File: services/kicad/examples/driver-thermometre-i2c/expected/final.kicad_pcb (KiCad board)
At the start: 2 copper layers, 40 x 40 mm, 10 parts, among them J1 CONN_5V_GND_SDA_SCL, U1 AMS1117-3.3

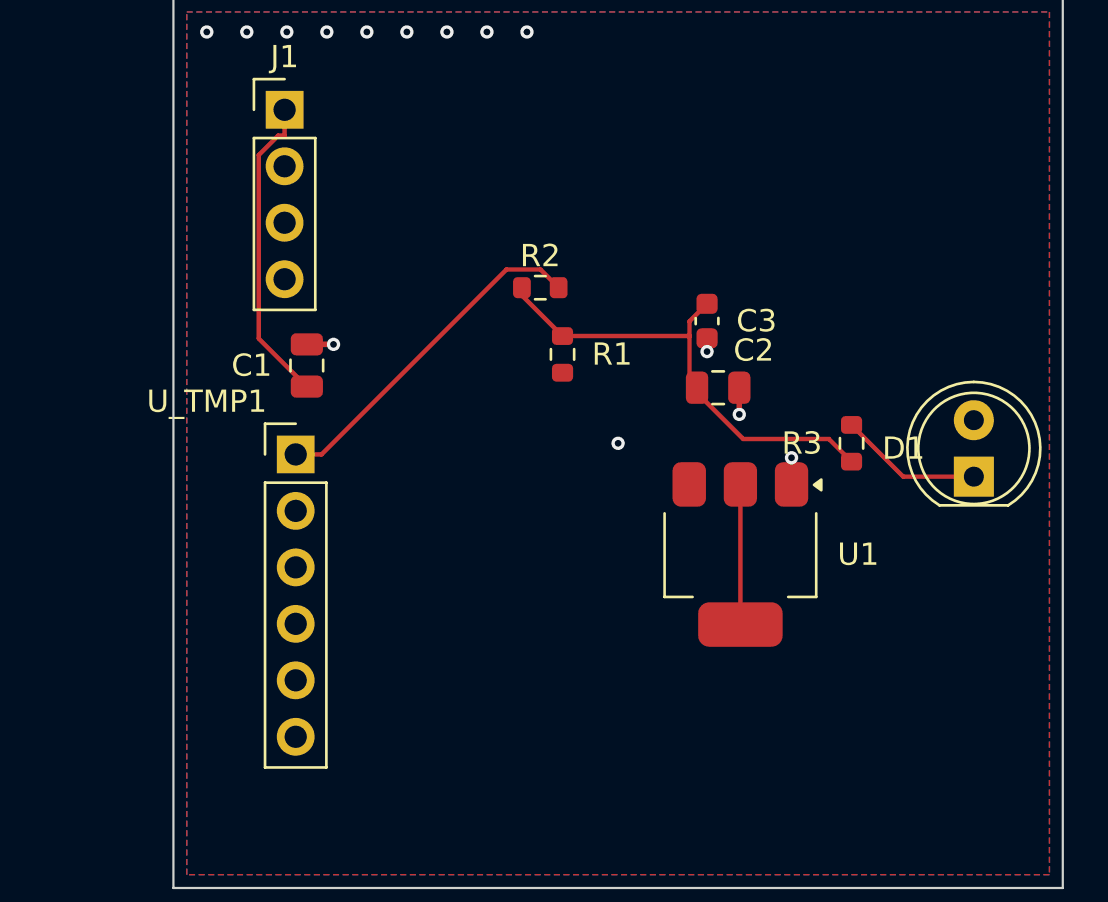
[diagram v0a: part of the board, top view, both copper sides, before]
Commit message: fix(agents): l'enrichissement ne reecrit plus un footprint deja qualifie ; exemple driver-thermometre-i2c sur le contrat durci
`quickLookup('J1', …)` rend un PinHeader 1x02 pour tout connecteur, quel que
soit l'indice : un footprint complet et juste (PinHeader_1x04) etait reecrit
en 1x02 dans l'etat publie et la BOM — le board, lui, gardait le bon. Un
footprint `Lib:Nom` ne se cherche plus.

Meme phrase rejouee sur le contrat durci (run 537dc8a5) : SDA passe de 1 a
3 broches, SCL de 2 a 3, 100 % route, 0 erreur, 198 s. README avant/apres.

Co-Authored-By: Claude Fable 5.1 <noreply@anthropic.com>
Claude-Session: https://claude.ai/code/session_01TnMqm4La2CxQHHB5K8aSSV
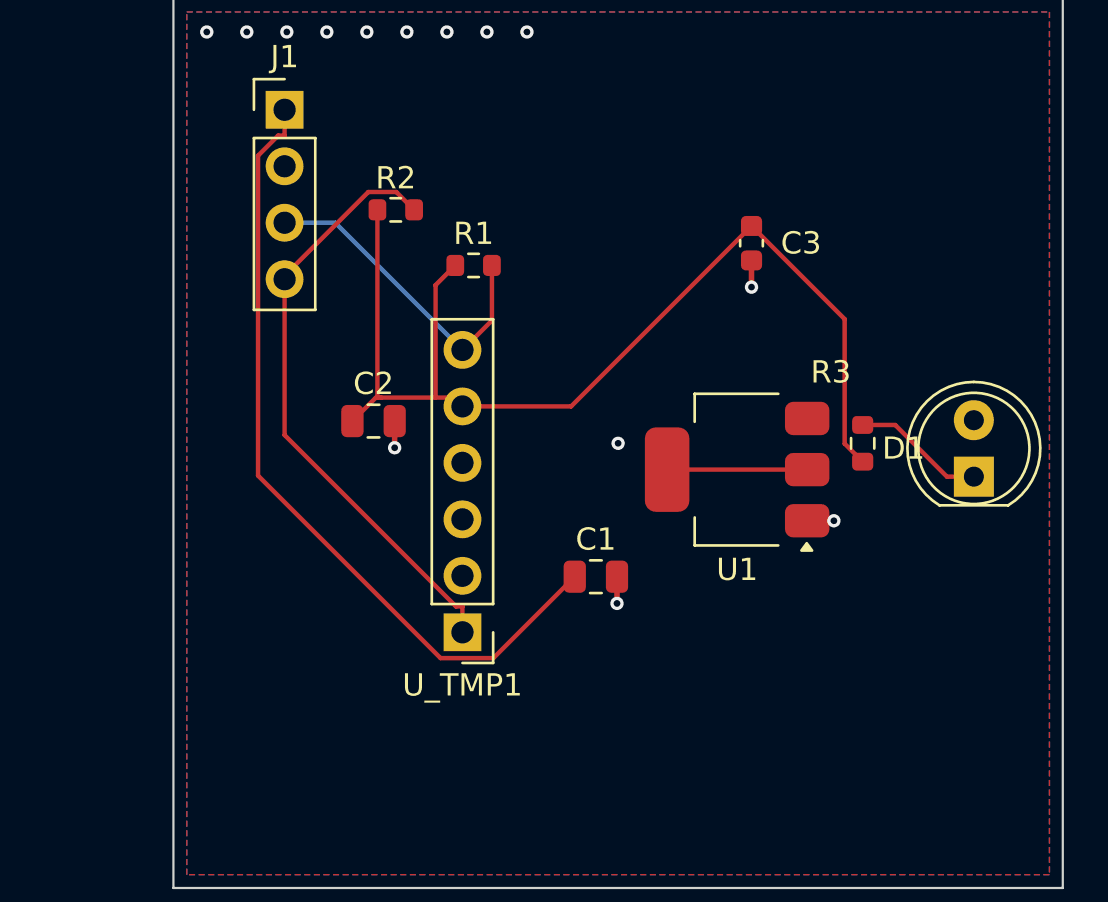
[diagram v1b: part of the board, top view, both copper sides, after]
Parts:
- J1: value CONN_5V_GND_SDA_SCL -> 5V_GND_SDA_SCL
- moved C1 16.1 mm to (147.5, 113.5), turned to 0 degrees
- moved C2 15.6 mm to (137.5, 106.5)
- moved U_TMP1 11.0 mm to (141.5, 116.0), turned to 180 degrees
- moved R2 7.38 mm to (138.5, 97.0)
- moved R1 5.66 mm to (142.0, 99.5), turned to 0 degrees
- moved C3 4.03 mm to (154.5, 98.5)
- moved U1 3.82 mm to (153.9, 108.7), turned to 180 degrees
- moved R3 0.50 mm to (159.5, 107.5)
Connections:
- J1 pad 3: Net-(J1-3) -> SDA
- J1 pad 4: Net-(J1-4) -> SCL
- U_TMP1 pad 4: Net-(U_TMP1-4) -> GND
- U_TMP1 pad 5: Net-(U_TMP1-5) -> +3V3
- U_TMP1 pad 6: Net-(U_TMP1-6) -> SDA
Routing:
- net +3V3: track 21.3 -> 49.3 mm
- net +5V: track 14.0 -> 36.3 mm
- net SDA: track 0.00 -> 14.7 mm
- net SCL: track 15.6 -> 27.2 mm
- net GND: track 4.20 -> 4.80 mm
- net NET_R3_D1: track 6.46 -> 5.96 mm

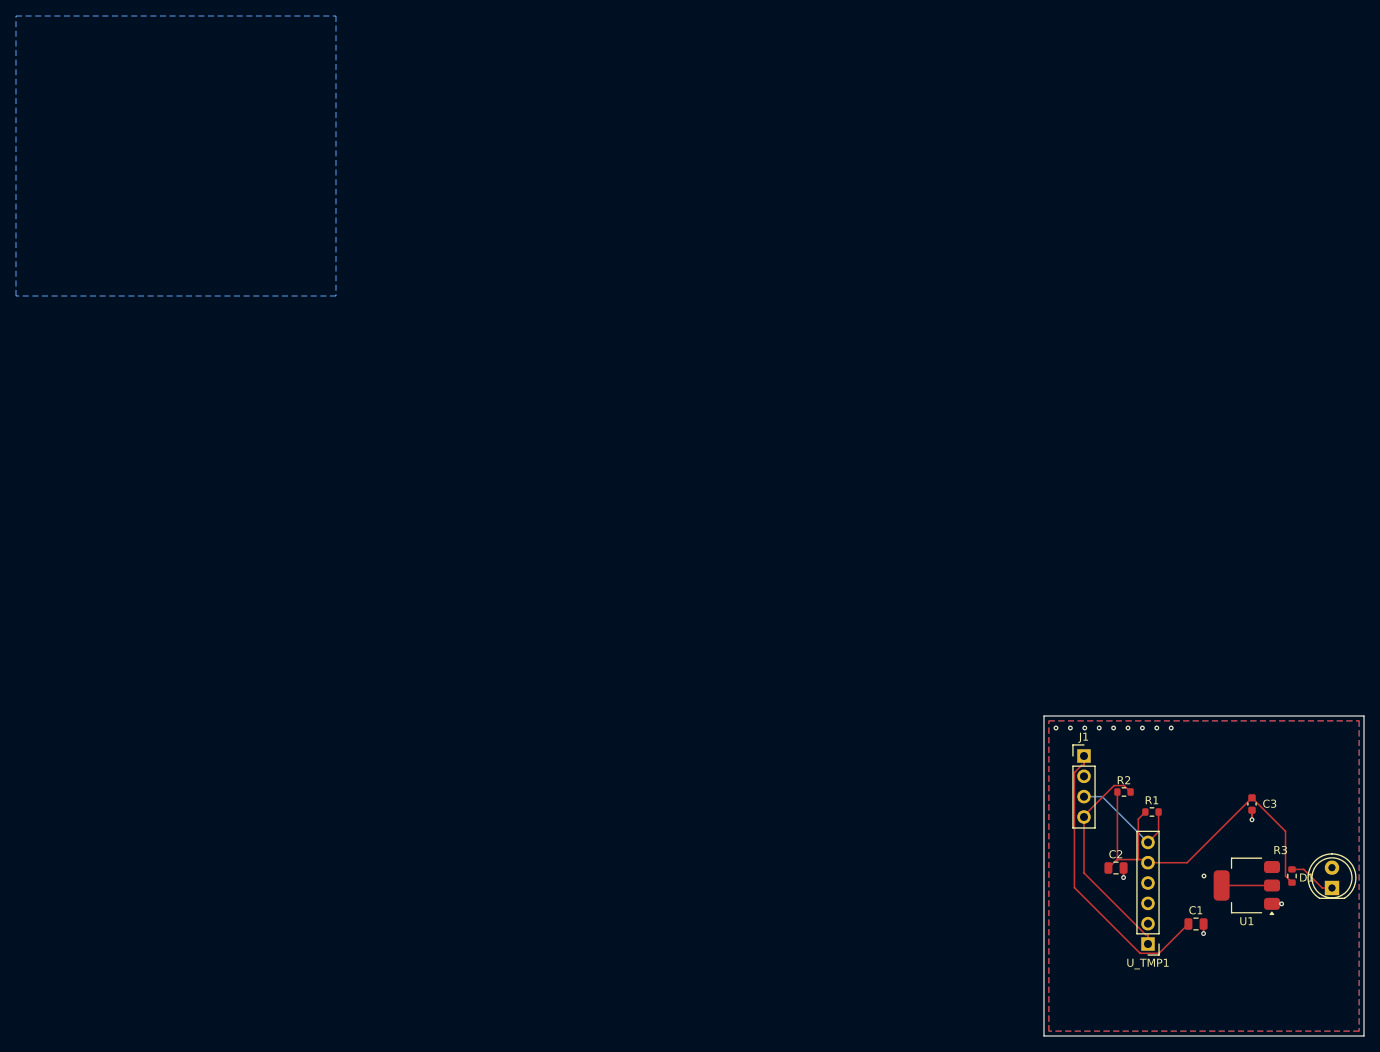
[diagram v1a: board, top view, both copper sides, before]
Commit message: banc(rejeu): douze cartes hors le banc des dix, et le trou qu elles ont revele
Demande : refaire placement et routage de toutes les cartes d `examples/`
SAUF les dix du banc, sans toucher `stm32-validation` ni `STM32-Test`.

DOUZE CARTES REJOUEES, DEUX FAMILLES.

  groupe A (input/schema.json)        regenerer_le_banc.py — garde le meilleur
      carte-11-croisements            100 % · 0 err · 0 perdu   GARDE
      driver-clignotant-ne555         100 % · 0 err · 0 perdu   GARDE
      driver-stm32-minimal            100 % · 0 err · 0 perdu   GARDE
      driver-thermometre-i2c          100 % · 0 err · 0 perdu   GARDE

  groupe B (input/circuit.json)       banc_exemples.py — ecrit dans output/
      arduino-uno       2 couches  100 %  0 manq  0 err    925 s
      esp32-baseline    2 couches  100 %  0 manq  0 err    387 s
      led-blinker       2 couches  100 %  0 manq  0 err    124 s
      nucleo-f401       4 couches   98 %  1 manq  0 err   1814 s
      stm32-baseline    2 couches  100 %  0 manq  0 err    193 s
      stm32-30          2 couches  100 %  0 manq  0 err    404 s
      stm32-60          2 couches  100 %  0 manq  0 err    414 s
      stm32-100         2 couches  100 %  0 manq  0 err    308 s

LE REJEU CONFIRME LES BOARDS LIVRES — ON NE REMPLACE RIEN.

DRC des boards VERSIONNES face aux boards du rejeu, meme instrument
(`kicad-cli pcb drc --severity-all`) des deux cotes :

      sept cartes            0 err · 0 manq des DEUX cotes   egalite
      nucleo-f401            0 manq versionne, 1 au rejeu    on garde l ancien

Livrer des boards de qualite identique ferait du bruit sans rien apporter, et
le tirage de `nucleo-f401` est moins bon : la protection a joue exactement
comme prevu.

LE TROU : CES HUIT CARTES N AVAIENT AUCUN `mesures.json`.

Leur board etait livre depuis le 2026-09-07 et RIEN ne disait ce qu il valait.
Un lecteur ne pouvait ni le verifier ni s en apercevoir — c est la faute que ce
depot poursuit partout, appliquee non pas a un compteur mais a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
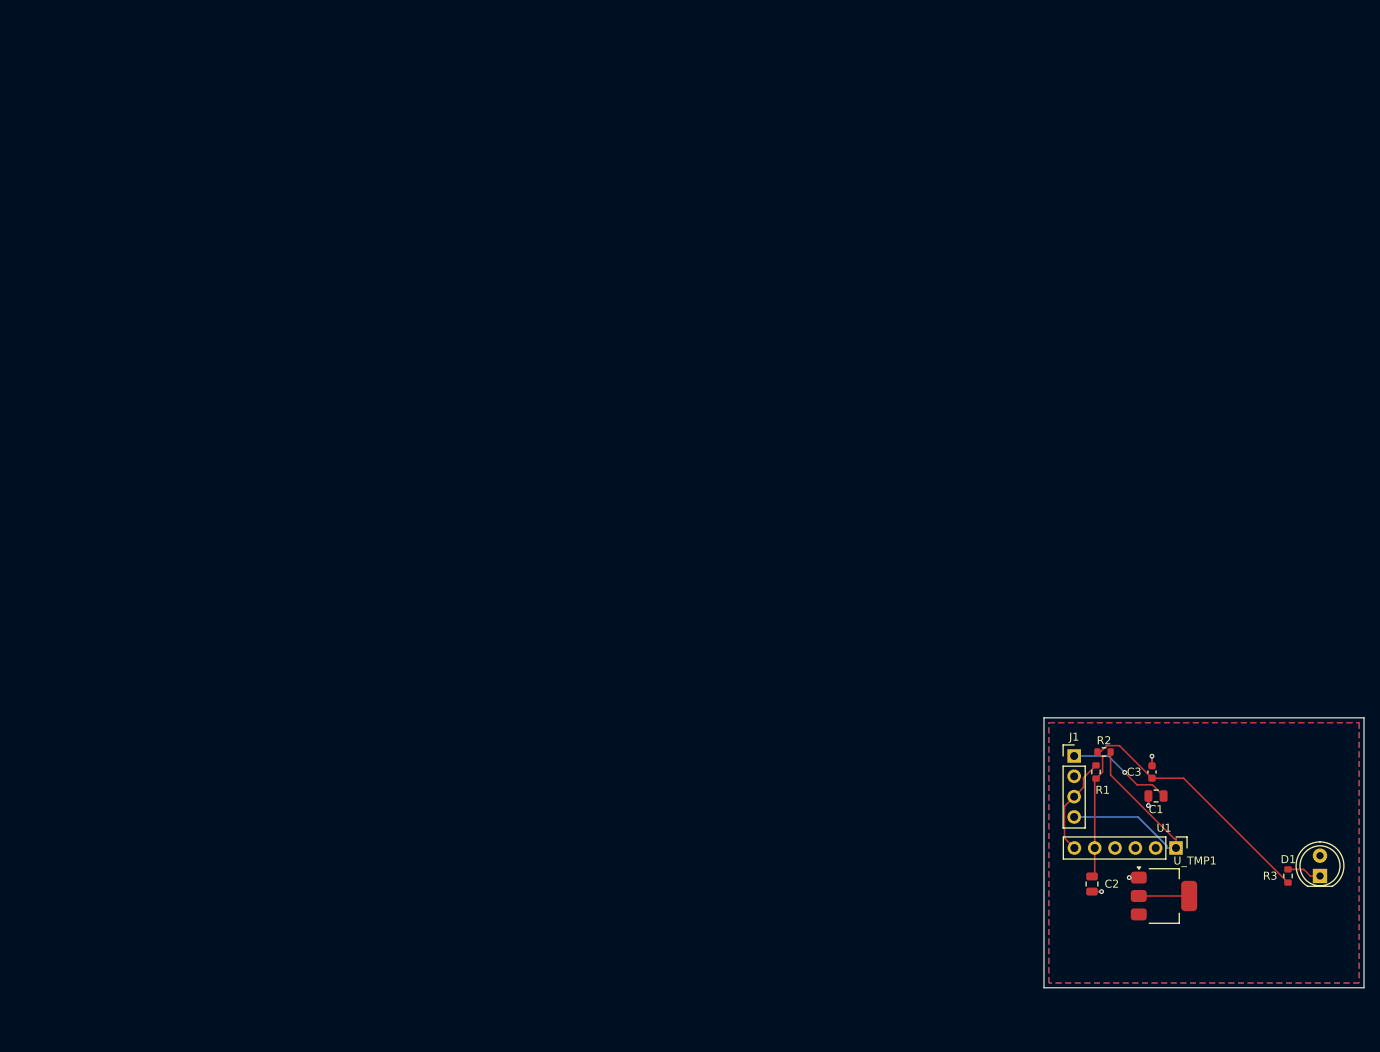
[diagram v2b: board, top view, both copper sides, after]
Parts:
- moved C1 16.8 mm to (142.5, 97.5), turned to 180 degrees
- moved C3 13.1 mm to (142.0, 94.5), turned to 90 degrees
- moved U_TMP1 12.5 mm to (145.0, 104.0), turned to -90 degrees
- moved U1 10.4 mm to (143.5, 110.0), turned to 0 degrees
- moved R1 8.60 mm to (135.0, 94.5), turned to 90 degrees
- moved R2 5.59 mm to (136.0, 92.0)
- moved C2 3.61 mm to (134.5, 108.5), turned to -90 degrees
- moved D1 2.12 mm to (163.0, 107.5)
- moved J1 1.23 mm to (132.3, 92.5)
- moved R3 0.50 mm to (159.0, 107.5)
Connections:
- net Net-(U1-3) renamed PWR_FLAG
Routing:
- net +5V: track 36.3 -> 13.3 mm, vias 0 -> 1
- net SCL: track 27.2 -> 30.0 mm
- net SDA: track 14.7 -> 12.5 mm
- net +3V3: track 49.3 -> 47.5 mm
- net NET_R3_D1: track 5.96 -> 4.34 mm
- net GND: vias 14 -> 4
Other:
- board size 40 x 40 mm -> 40 x 33.7 mm
